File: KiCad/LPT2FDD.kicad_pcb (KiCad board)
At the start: 2 copper layers, 30 x 54.5 mm, 2 parts, among them J1 Floppy Connector, J2 LPT Floppy

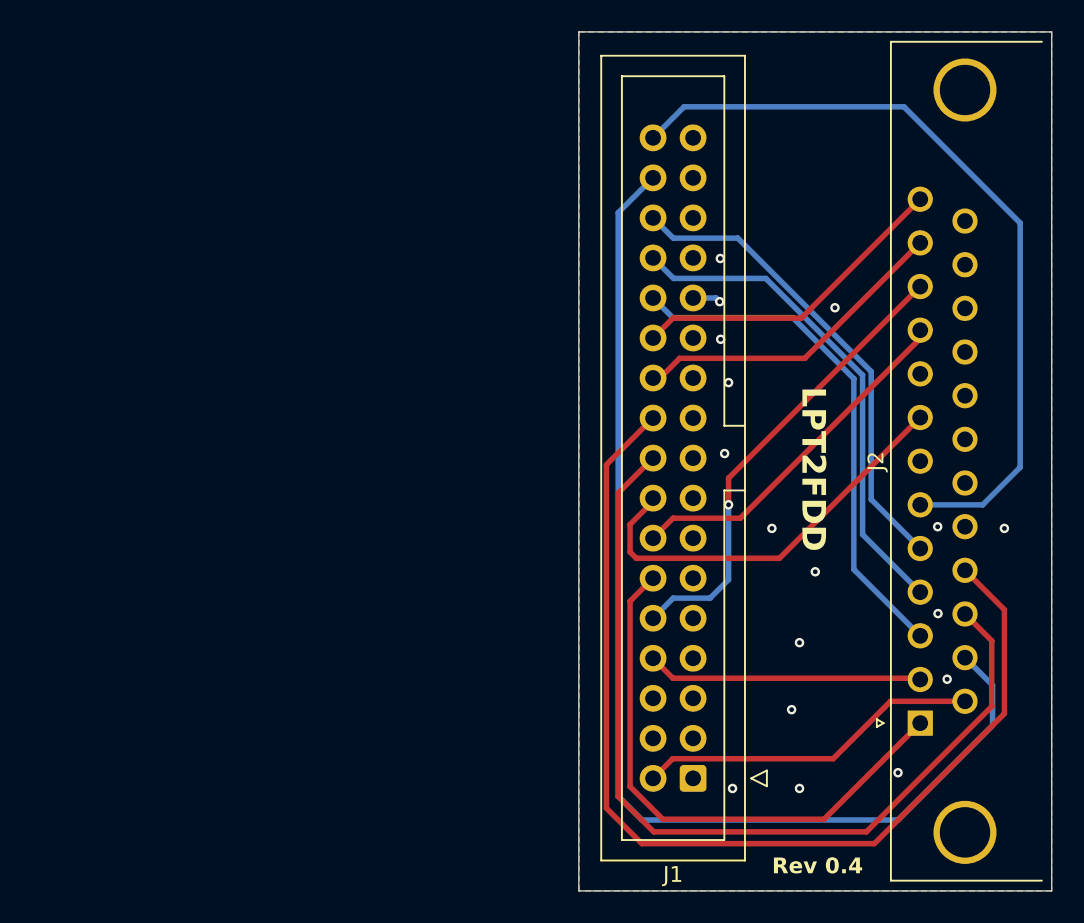
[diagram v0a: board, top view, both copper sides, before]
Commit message: v0.5 Add pin 21 and pin 22 jumper for Compaq compatibility
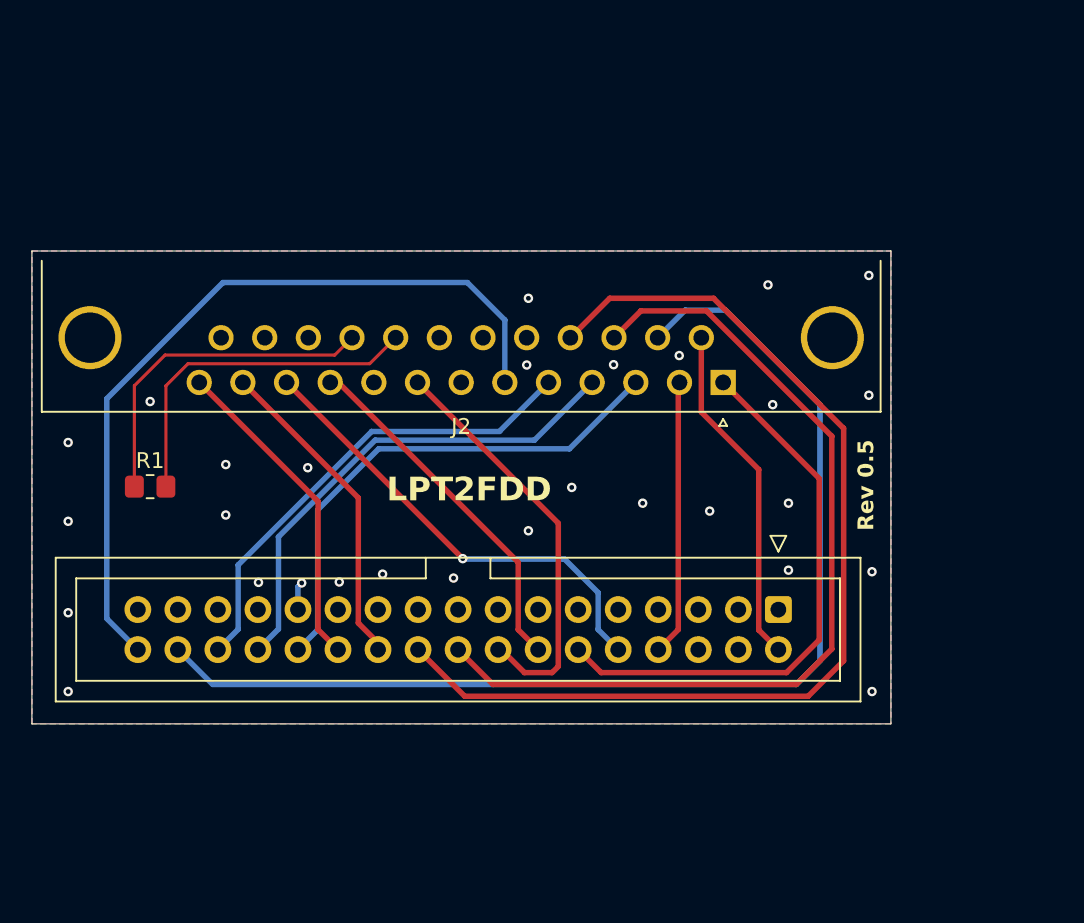
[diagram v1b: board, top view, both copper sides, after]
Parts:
- added R1: 1k, Resistor_SMD:R_0805_2012Metric_Pad1.20x1.40mm_HandSolder, F.Cu at (131.6, 95.3)
- moved J2 25.0 mm to (167.9, 88.7), turned to 180 degrees
- moved J1 12.0 mm to (171.4, 103.2), turned to -90 degrees
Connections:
- J2 pad 21: GND -> Net-(J2-P21)
- J2 pad 22: GND -> Net-(J2-P22)
- J2 pad 25: GND -> VCC
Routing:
- net Net-(J2-P21): track 0.00 -> 22.2 mm
- net Net-(J2-P22): track 0.00 -> 21.5 mm
- net GND: vias 17 -> 29
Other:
- board size 30 x 54.5 mm -> 54.5 x 30 mm
- board text added: "Rev 0.5"
- board text removed: "Rev 0.4"
